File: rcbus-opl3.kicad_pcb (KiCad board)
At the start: 2 copper layers, 100 x 50 mm, 38 parts, among them CON1 3.5mm jack, P1 RC2014 BUS, U1 TL074, U2 YAC512, U3 74HCT688, U4 YMF262, Y1 14.3181MHz

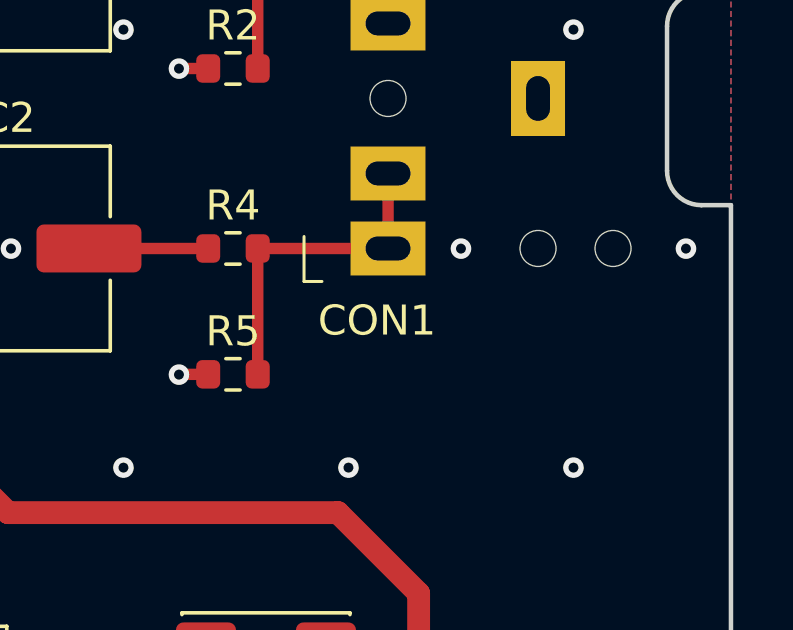
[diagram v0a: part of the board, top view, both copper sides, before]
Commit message: add datasheets / farnell links
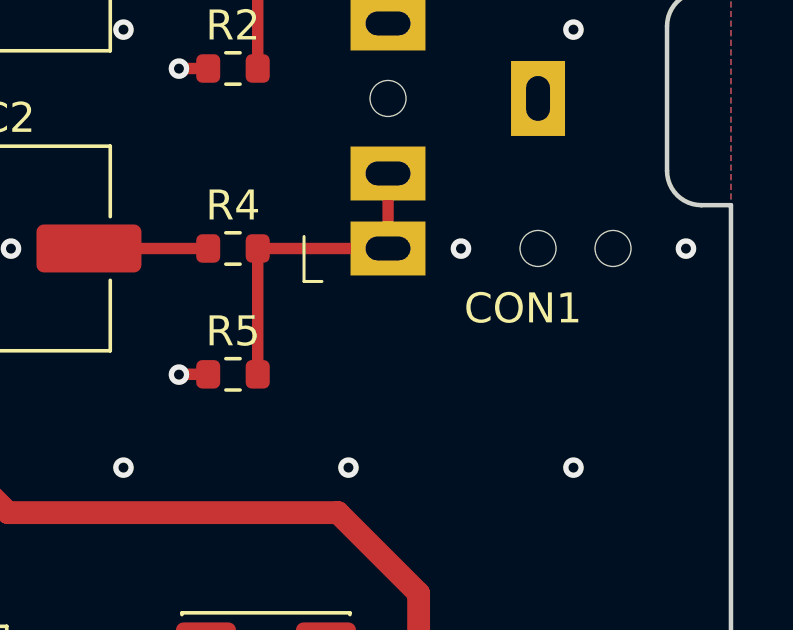
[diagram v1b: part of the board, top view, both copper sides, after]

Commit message: add mpn field
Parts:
- JP1: value BASE ADDRESS -> 2x06 pin header
- P1: value RC2014 BUS -> 1x39 pin header

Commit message: some r2 changes
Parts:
- U2: footprint Package_SO:SOP-16_4.55x10.3mm_P1.27mm -> Package_SO:SOIC-16W_5.3x10.2mm_P1.27mm
- moved G2 1.27 mm to (93.8, 123.0)
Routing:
- net GND: track 32.7 -> 33.6 mm
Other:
- board text added: "RCBus OPL3 sound card"
- board text removed: "RCBus OPL3 Sound Card"

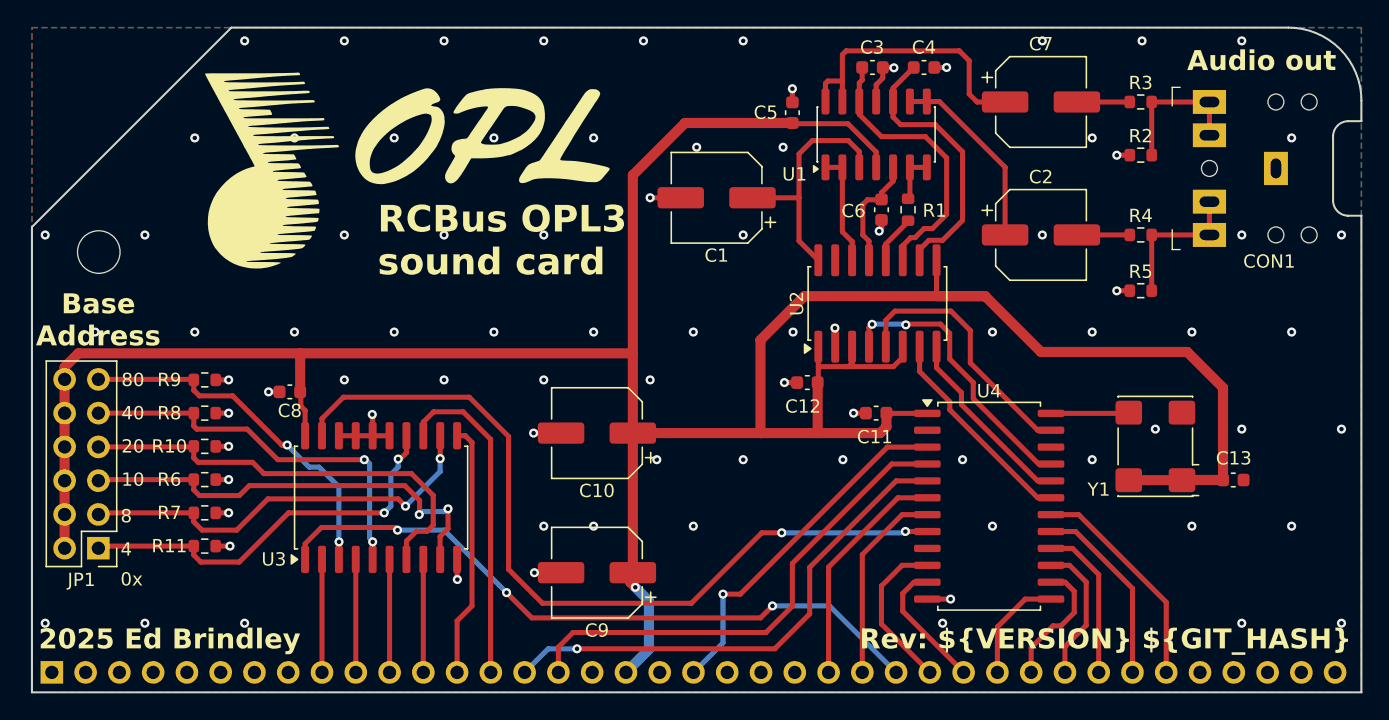
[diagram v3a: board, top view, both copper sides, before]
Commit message: wip: change 10uf electrolytics to 4mm diameter, and use custom footprint for ymf262
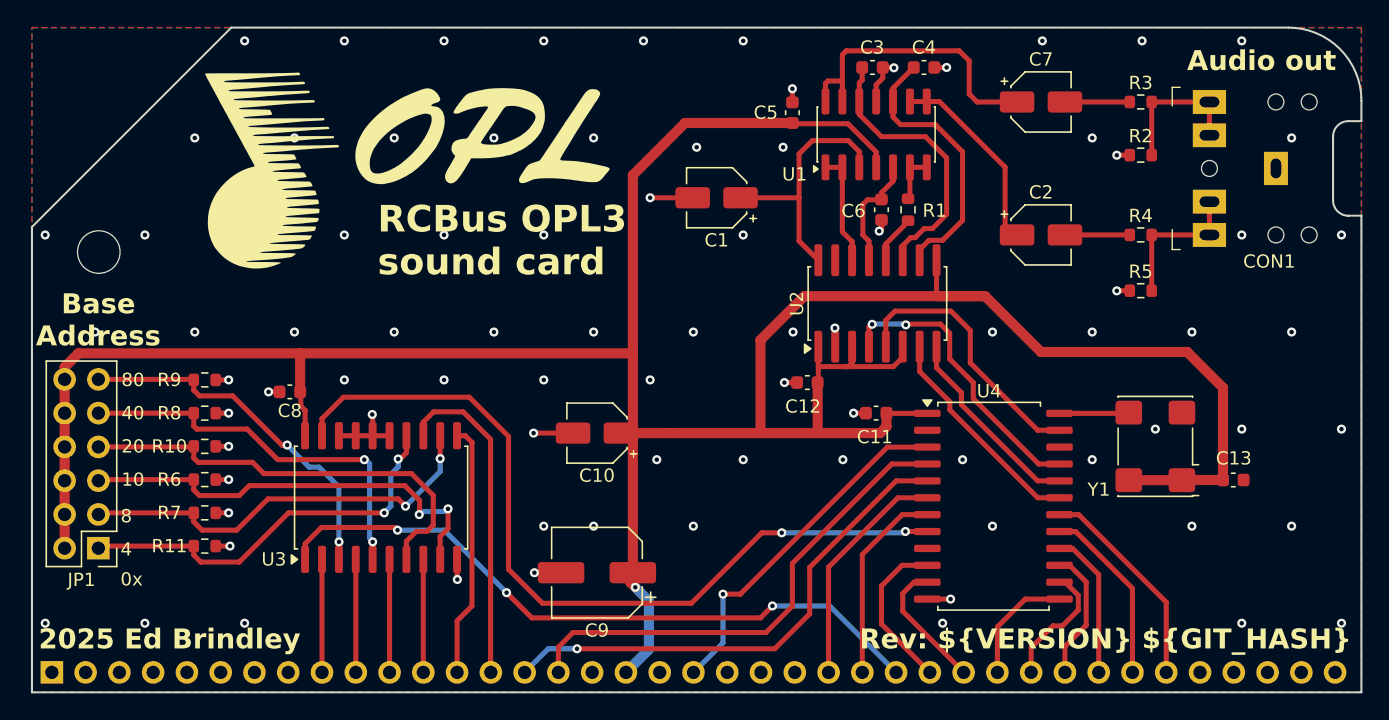
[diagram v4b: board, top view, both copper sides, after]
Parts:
- C1, C10, C2, C7: footprint Capacitor_SMD:CP_Elec_6.3x5.8 -> Capacitor_SMD:CP_Elec_4x5.4
- U4: footprint Package_SO:SOP-24_7.5x15.4mm_P1.27mm -> electrified:SOP-24_wider
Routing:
- net GND: vias 86 -> 85

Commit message: fix drc, reroute for new width components, add pin 1 indicator for oscillator
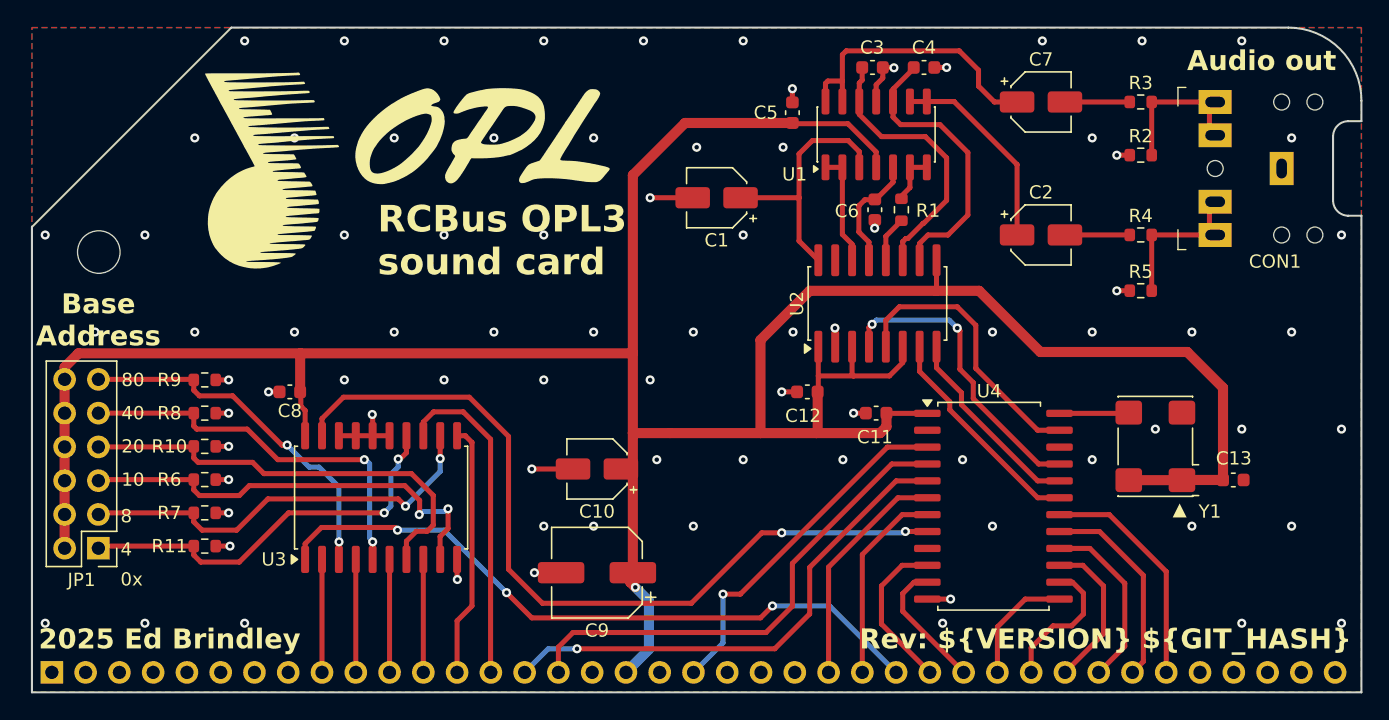
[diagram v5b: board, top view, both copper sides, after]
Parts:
- moved C10 2.70 mm to (102.5, 148.2)
- moved C12 0.70 mm to (118.3, 142.4)
- moved C6 0.50 mm to (123.4, 128.7)
- moved R1 0.50 mm to (125.4, 128.7)
- moved CON1 0.43 mm to (149.0, 125.6)
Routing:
- net +5V: track 229.1 -> 226.3 mm
- net /D5: track 11.8 -> 14.1 mm
- net /D6: track 14.2 -> 16.0 mm
- net /D4: track 10.6 -> 12.3 mm
- net /D7: track 16.7 -> 18.0 mm
- net /R: track 14.1 -> 15.3 mm
- net /D3: track 9.59 -> 10.6 mm
- net Net-(U1B-+): track 8.26 -> 9.08 mm
- net /AUDIO_CH1: track 20.8 -> 21.6 mm
- net /DOAB: track 21.5 -> 22.3 mm
- net /L: track 21.7 -> 20.9 mm
- net /DAC_CLK: track 19.8 -> 20.6 mm
- net GND: track 33.6 -> 33.9 mm, vias 85 -> 84
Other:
- board text added: "▲"

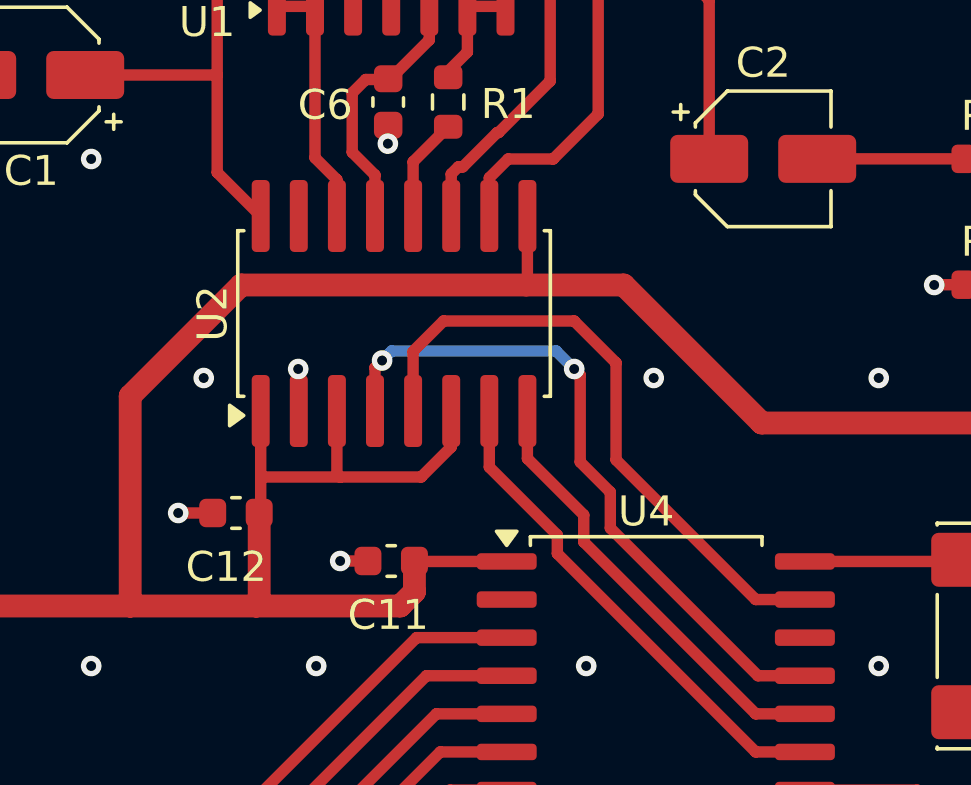
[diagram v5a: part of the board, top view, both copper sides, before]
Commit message: update symbols/footprints to kicad 9.0.7, improve ymf footprint
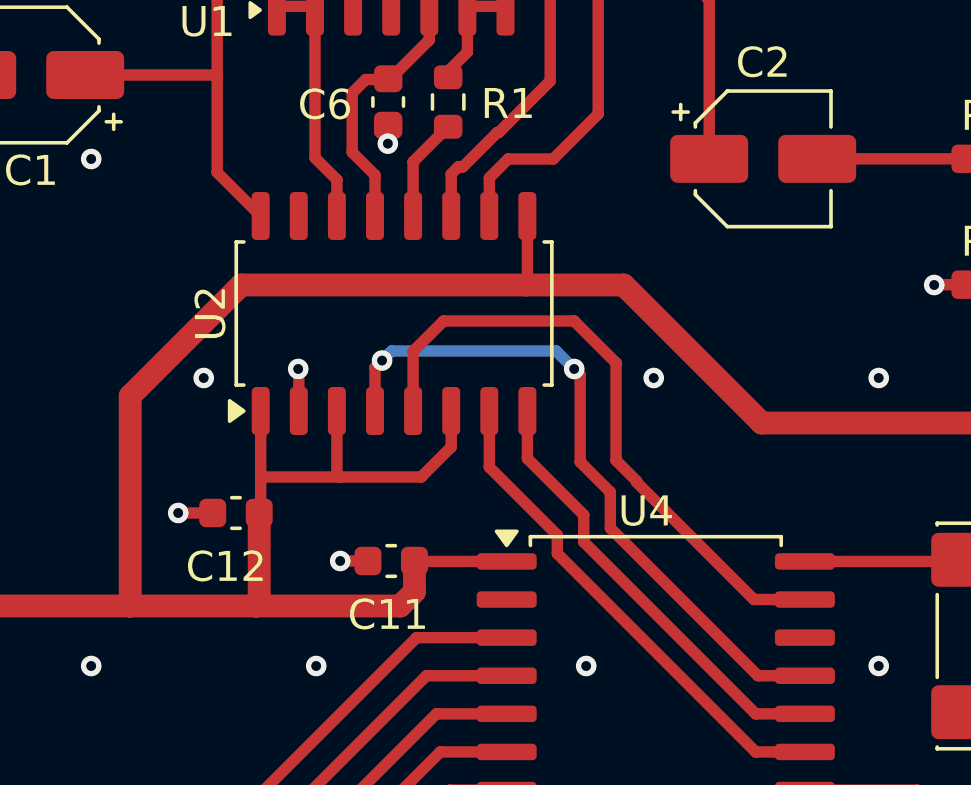
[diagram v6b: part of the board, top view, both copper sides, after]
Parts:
- U2: footprint Package_SO:SOIC-16W_5.3x10.2mm_P1.27mm -> Package_SO:SOP-16_4.55x10.3mm_P1.27mm
